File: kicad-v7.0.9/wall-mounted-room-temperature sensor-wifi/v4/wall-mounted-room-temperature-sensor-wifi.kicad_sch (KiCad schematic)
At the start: 50 parts, among them J1 dc_barrel_jack, P1 2x3_pins_header, P2 1x9_pinsocket, Q1 DMG2307L, SW1 TVAF18BB, SW2 TVAF18BB, SW3 B3F-4150, SW4 B3F-4150, SW5 B3F-4150, U1 TPS79633KTTR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

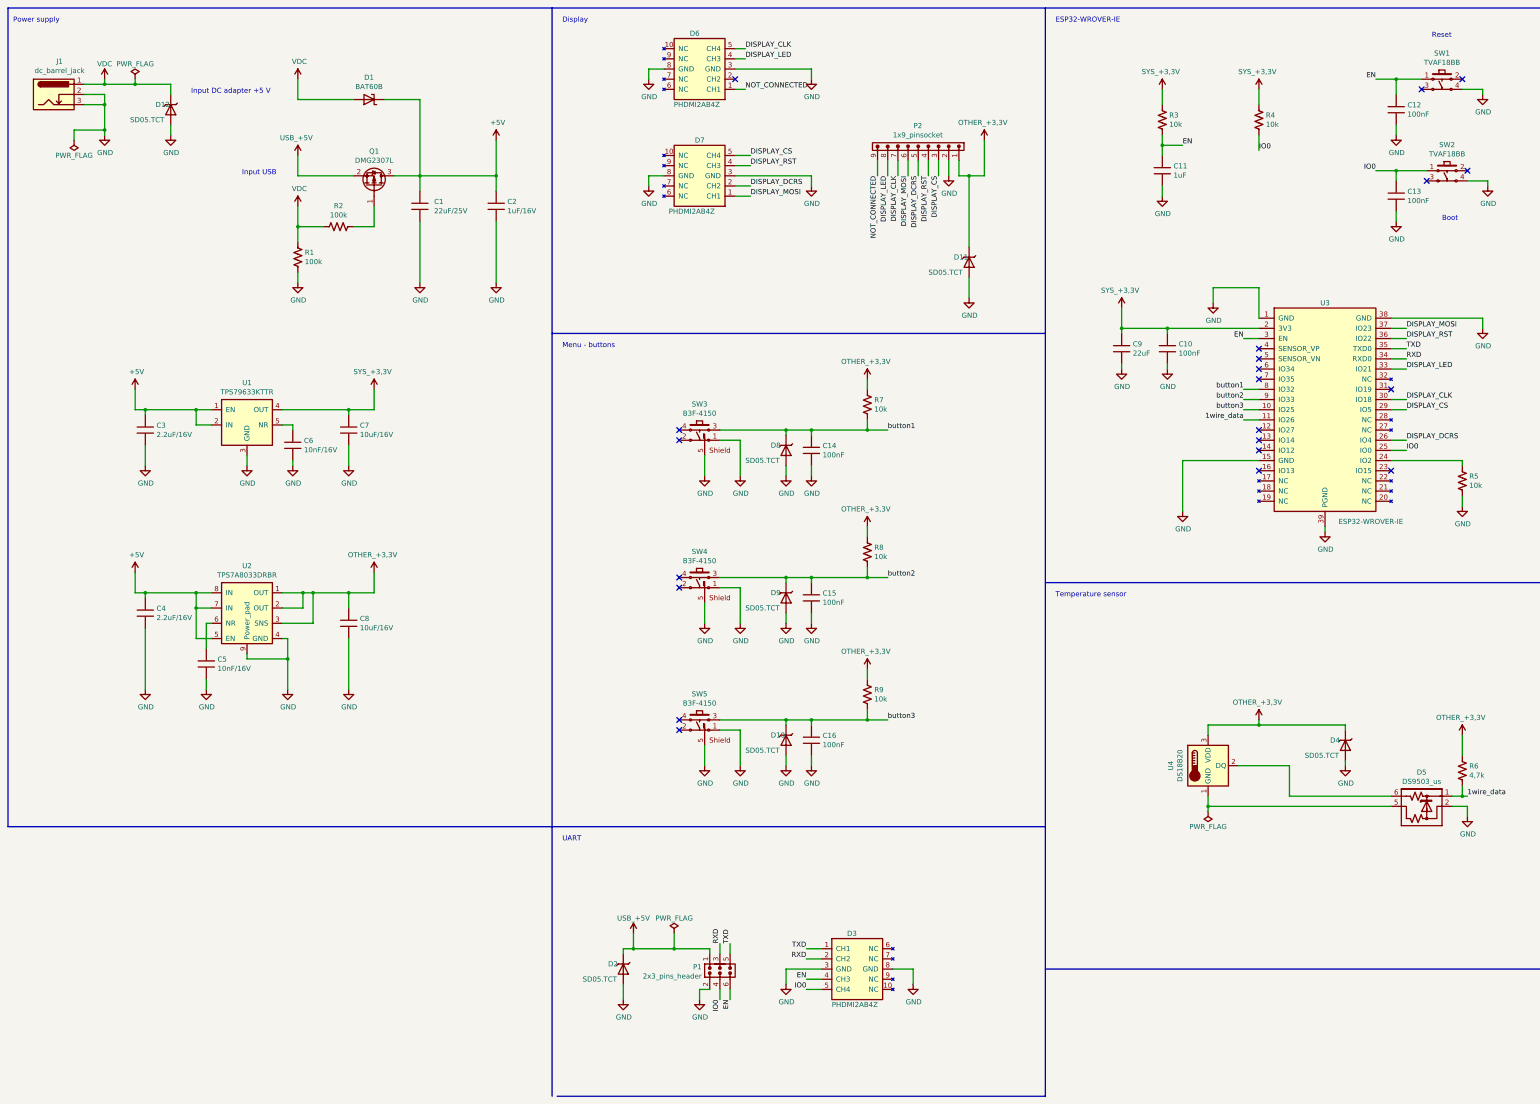
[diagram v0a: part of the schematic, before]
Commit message: Wall mounted room temperature sensor - WiFi. Small changes in schematic a PCB.
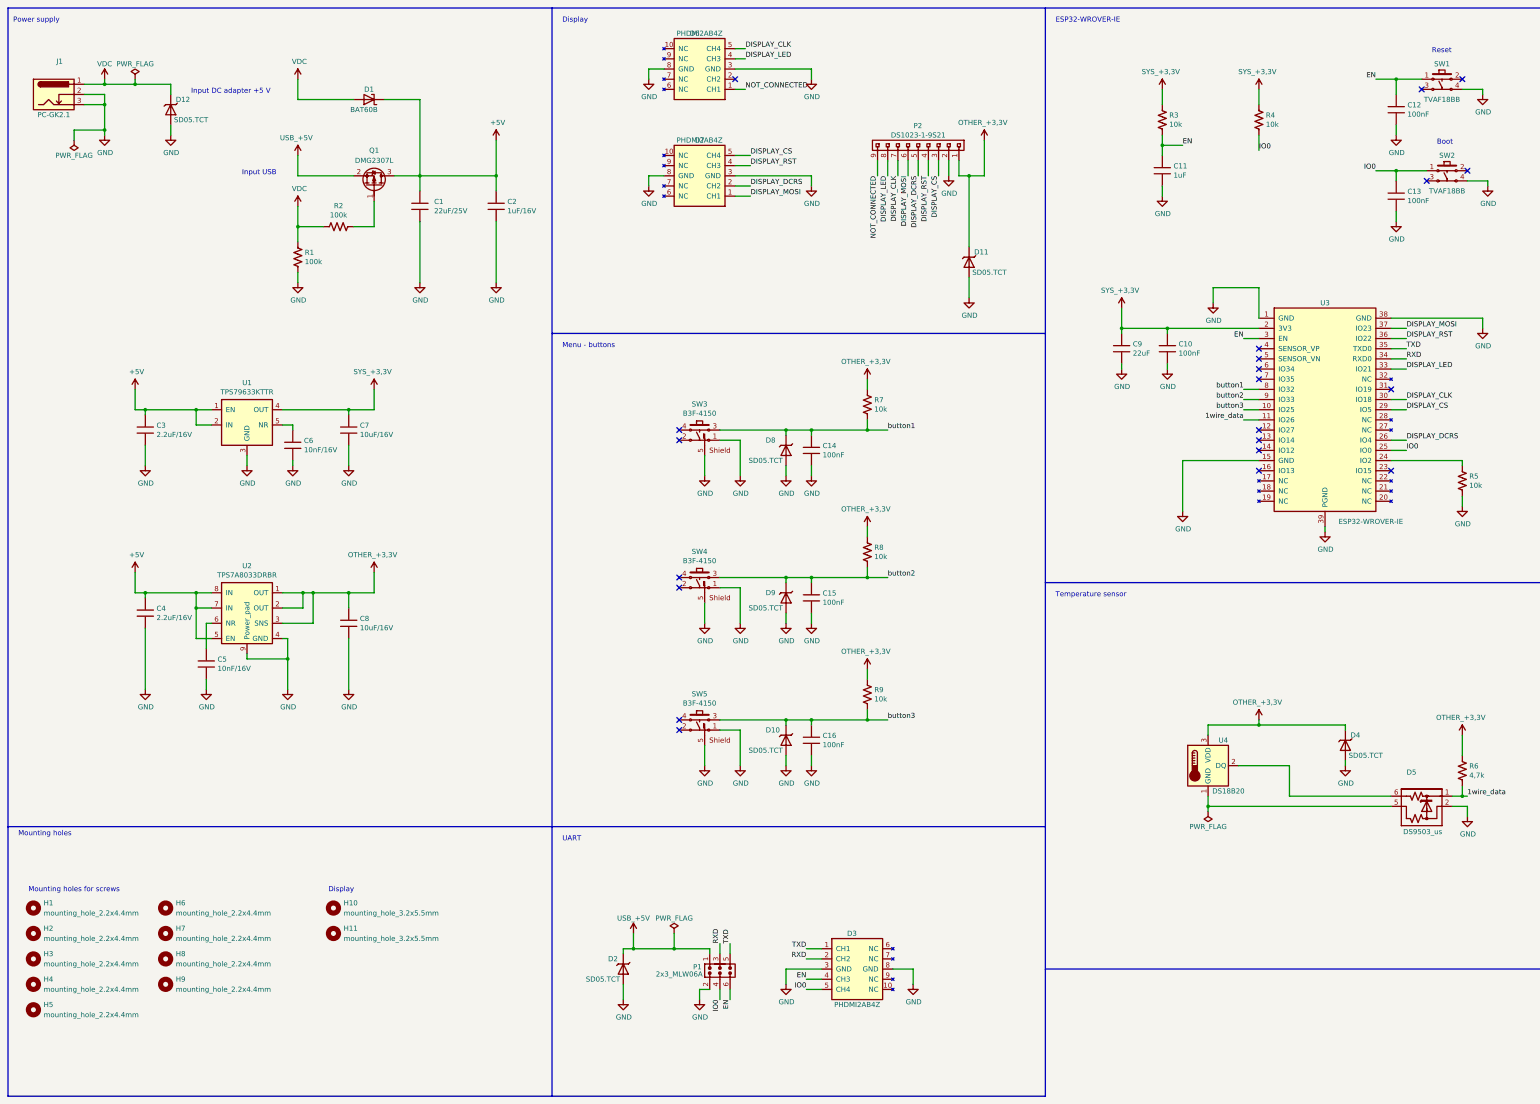
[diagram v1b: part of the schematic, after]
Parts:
- added H1, H2, H3, H4, H5, H6, H7, H8, H9: mounting_hole_2.2x4.4mm, mounting_hole_rl:mounting_hole_2.2x4.4mm, symbol mounting_hole_rl:mounting_hole_2.2x4.4mm
- added H10, H11: mounting_hole_3.2x5.5mm, mounting_hole_rl:mounting_hole_3.2x5.5mm, symbol mounting_hole_rl:mounting_hole_3.2x5.5mm
- C1, C10, C11, C12, C13, C14, C15, C16, C2, C3, C4, C5, C6, C7, C8, C9: symbol passive_component_rl:capacitor -> capacitor_smd_rl:c_0805
- D1: symbol diode_rl:schottky_diode -> diode_smd_rl:BAT60B
- D10, D11, D12, D2, D4, D8, D9: symbol diode_rl:undir_transil -> transil_diode_smd_rl:SD05.TCT
- D3, D6, D7: symbol diode_rl:PUSB3AB4 -> transil_diode_smd_rl:PHDMI2AB4Z
- D5: symbol diode_rl:DS9503_us -> transil_diode_smd_rl:DS9503_us
- J1: value dc_barrel_jack -> PC-GK2.1; footprint dc_barrel_jack_rl:PC-GK2.1 -> dc_barrel_jack_tht_rl:PC-GK2.1; symbol connector_rl:dc_barrel_jack -> dc_barrel_jack_tht_rl:PC-GK2.1
- P1: value 2x3_pins_header -> 2x3_MLW06A; symbol connector_rl:2x3_pins_header -> connector_idc_rl:2x3_MLW06A
- P2: value 1x9_pinsocket -> DS1023-1-9S21; symbol connector_rl:1x9_pin_socket -> connector_tht_pin_socket_2.54mm_rl:DS1023-1-9S21
- Q1: symbol wall-mounted-room-temperature-sensor-wifi-rescue:p_mosfet-unipolar_transistor_rl -> unipolar_transistor_smd_rl:DMG2307L
- R1, R2, R3, R4, R5, R6, R7, R8, R9: symbol passive_component_rl:resistor_us -> resistor_smd_rl:r_0805_us
- SW1, SW2: symbol microswitch_rl:TVAF18BB -> microswitch_smd_rl:TVAF18BB
- SW3, SW4, SW5: symbol microswitch_rl:B3F-4150 -> microswitch_tht_rl:B3F-4150
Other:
- note added: "Mounting holes"
- note added: "Mounting holes for screws"
- moved on the sheet: D1, Q1
